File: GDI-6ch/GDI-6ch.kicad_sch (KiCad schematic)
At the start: 245 parts, among them J1 Conn_02x02_Odd_Even, J2 FTSH-107-01-F-DV-K, J3 TC2030, J4 Conn_01x06, J5 Conn_01x04, P1 368255-2, P10 Pad, P11 Pad, P18 Pad, P19 Pad, P2 Pad, P20 Pad, P25 Pad, P26 Pad, P27 Pad, P28 Pad, P29 Pad, P3 Pad, P30 Pad, P31 Pad, P32 Pad, P36 Pad, P4 Pad, P5 Pad, P6 Pad, P7 Pad, P8 Pad, P9 Pad, Q10 BUK9230-100B, Q11 BUK9230-100B, Q12 BUK9230-100B, Q13 AOD4185, Q14 VND14NV04TR-E, Q15 VND14NV04TR-E, Q2 BUK9230-100B, Q3 BUK9230-100B, Q4 BUK9230-100B, Q5 BUK9230-100B, Q6 BUK9230-100B, Q7 BUK9230-100B, Q8 BUK9230-100B, Q9 BUK9230-100B, U1 MC33816, U2 TJA1051T-3, U3 LM78M05_TO252, U4 74HC14, U5 XC6206P332MR, U6 MCP6004, U7 STM32F103C8Tx, Y2 1MHz

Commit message: Upd SCH
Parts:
- removed P11, P25, P26, P27, P28, P29, P30, P31, P6: Pad, hellen-one-common:PAD-TH, symbol hellen-one-common:Pad
- removed U1: MC33816, kicad6-libraries:LQFP-64-1EP_10x10mm_P0.5mm_EP5x5mm_ThermalVias, symbol chips:MC33816
- added C84, C85, C87, C88, C93, C94, C95, C96: 1000pF, Capacitor_SMD:C_0603_1608Metric, symbol Device:C
- added C86: 100n, hellen-one-common:C0603, symbol hellen-one-common:Cap
- added C89, C90, C91, C92: 4700p, hellen-one-common:C0603, symbol hellen-one-common:Cap
- added C97, C98: 0.33uF, Capacitor_SMD:C_0603_1608Metric, symbol Device:C
- added C99: 330p, hellen-one-common:C0603, symbol hellen-one-common:Cap
- added D17: SBR10200CTL, Package_TO_SOT_SMD:TO-252-2, symbol Device:D_Schottky_Dual_CommonCathode_AKA
- added D19, D22: STPS2H100UY, Diode_SMD:D_SMB, symbol Device:D_Schottky_Small
- added Q1, Q16, Q17, Q18: BUK9230-100B, Package_TO_SOT_SMD:TO-252-2, symbol Device:Q_NMOS_GDS
- added R37, R41, R84, R85, R86, R87: Jumper-Pad-Pad, hellen-one-common:PAD-0805-PAD, symbol hellen-one-common:Jumper-Pad-Pad
- added R88, R89: 1K, Resistor_SMD:R_0603_1608Metric, symbol Device:R
- added R90: 0.01, kicad6-libraries:Shunt_1206, symbol Device:R_Shunt
- added R91, R92, R93, R94: 10, Resistor_SMD:R_0603_1608Metric, symbol Device:R
- added R95, R96: DNP, hellen-one-common:PAD-0805-PAD, symbol hellen-one-common:Jumper-Pad-Pad
- added U1: 74HC14, Package_SO:TSSOP-14_4.4x5mm_P0.65mm, symbol 74xx:74HC14
- added U8: PT2000, kicad6-libraries:LQFP-80-1EP_12x12mm_P0.5mm, symbol chips:PT2000
- F1: LCSC C310989 -> C310992; MyComment 10A -> 20A
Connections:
- net +3V3: now also C86.2, R88.1, R89.1, U1.14 (VCC)
- net +5V: now also U8.22 (VCC5)
- net +BATT: now also Q1.2 (D), U8.47 (VBAT)
- net CLK: now also U8.80 (CLK)
- net CSB: now also U8.14 (CS)
- net DRVEN: now also U8.1 (DRVEN)
- net FLAG_0: now also U8.10 (FLAG0/EXTFW1)
- net GND: now also C84.1, C85.1, C86.1, C87.1, C88.1, C89.1, C90.1, C91.1, C92.1, D17.1 (A), R90.4, U1.11, U1.13, U1.5, U1.7 (GND), U1.9, U8.20 (DGND), U8.23 (AGND), U8.81 (PGND_(EXPOSED_PAD))
- net H1: now also U8.75 (S_HS2)
- net H3: now also U8.69 (S_HS4)
- net H5: now also C89.2, C90.2, C94.1, C98.2, D17.2 (K), Q16.3 (S), R85.2, R87.2, U8.63 (S_HS6); no longer C62.1, C64.2, C65.2, D15.1 (K), Q11.3 (S)
- net IN_PUMP1: now also C29.2, R27.2, RN2.4 (R4.1); no longer C18.2, R8.2, RN2.3 (R3.1)
- net IN_PUMP2: now also C18.2, R8.2, RN2.3 (R3.1); no longer C29.2, R27.2, RN2.4 (R4.1)
- net L1: now also U8.46 (D_LS1)
- net L2: now also U8.45 (D_LS2)
- net L3: now also U8.44 (D_LS3)
- net L4: now also U8.43 (D_LS4)
- net L5: now also C91.2, D19.2 (A), Q17.2 (D), R84.2, U8.42 (D_LS5); no longer C67.2, D16.2 (A), Q12.2 (D)
- net LS1: now also U7.45 (PB8); no longer U7.11 (PA1)
- net MISO: now also U8.16 (MISO)
- net MOSI: now also U8.15 (MOSI)
- net OA_1: now also U8.36 (OA_1)
- net OA_2: now also U8.37 (OA_2/FLAG_14)
- net RESETB: now also U8.2 (RESET)
- net SCLK: now also U8.17 (SCK)
- net START1: now also U8.3 (START1/FLAG_5)
- net START2: now also U8.4 (START2/FLAG_6)
- net START3: now also U8.5 (START3/FLAG_7)
- net START4: now also U8.6 (START4/FLAG_8)
- net START5: now also U8.7 (START5/FLAG_9)
- net START6: now also U8.8 (START6/FLAG_10)
- net VCCP: now also U8.48 (VCCP)
- net Vdrive: now also D19.1 (K), D22.1 (K), Q16.2 (D), U8.57 (VBOOST)
- net Vdrive_coil: now also U8.40 (D_LS7)
- net at C40.2, C56.1, D11.3 (A)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: now also U8.72 (S_HS3)
- net at C39.2, C52.1, D10.3 (A)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: now also U8.78 (S_HS1)
- net at C39.1: now also U8.76 (B_HS1)
- net FLAG_3: now reaches U7.38 (PA15)
- net FLAG_3: now also R96.2
- net at C51.2, D8.4, RN2.5 (R4.2): now also U1.3; no longer U4.13
- net at C10.2, R21.2: now also U8.27 (VSENSEP1)
- net at C10.1, R21.3: now also U8.26 (VSENSEN1)
- net at R81.1: now also U8.11 (FLAG1/EXTFW2)
- net at P1.45: now also R37.1
- net at P1.47: now also R41.1
- net at C13.1, R26.3: now also U8.30 (VSENSEN3)
- net at C13.2, R26.2: now also U8.31 (VSENSEP3)
- net at C59.2, R45.4: now also U8.18 (VCCIO)
- net at C24.1, R12.3: now also U8.32 (VSENSEN5)
- net at C24.2, R12.2: now also U8.33 (VSENSEP5)
- net OUT_INJ5_N: now reaches P1.117
- net OUT_INJ5_N: now also R86.1
- net OUT_INJ6_N: now reaches P1.115
- net OUT_INJ6_N: now also R84.1
- net OUT_INJ5_P: now reaches P1.116
- net OUT_INJ5_P: now also R85.1
- net OUT_INJ6_P: now reaches P1.120
- net OUT_INJ6_P: now also R87.1
- net IN_INJ5: now reaches RN2.1 (R1.1)
- net IN_INJ5: now also C84.2, R37.2, R88.2
- net IN_INJ6: now reaches RN2.2 (R2.1)
- net IN_INJ6: now also C85.2, R41.2, R89.2
- net at C37.2, D8.6, RN2.6 (R3.2): now also U1.1; no longer U4.11
- net at RN2.7 (R2.2): now also U4.13, C88.2
- net at RN2.8 (R1.2): now also U4.11, C87.2
- net at C32.2, C9.2: now also U8.21 (VCC2P5)
- net at R14.1: now also U8.55 (G_LS2)
- net at R11.1: now also U8.74 (G_HS2)
- net at R80.1: now also U8.79 (IRQ/FLAG_13)
- net at R10.1: now also U8.77 (G_HS1)
- net at C64.1: now also U8.58 (B_HS7)
- net at R82.1: now also U8.12 (FLAG2/EXTFW3)
- net at R83.1: now also U8.19 (DBG/FLAG_15)
- net at C11.1, R22.3: now also U8.28 (VSENSEN2)
- net at C11.2, R22.2: now also U8.29 (VSENSEP2)
- net at R24.2: now also U8.50 (G_LS7)
- net at R20.1: now also U8.49 (G_LS8)
- net at R18.1: now also U8.53 (G_LS4)
- net at R17.1: now also U8.54 (G_LS3)
- net at R13.1: now also U8.56 (G_LS1)
- net at R19.1: now also U8.59 (G_HS7)
- net at C42.1: now also U8.67 (B_HS4)
- net at R16.1: now also U8.68 (G_HS4)
- net at C40.1: now also U8.70 (B_HS3)
- net at R15.1: now also U8.71 (G_HS3)
- net at C41.1: now also U8.73 (B_HS2)
- net FLAG_4: now reaches U7.5 (PD0)
- net FLAG_4: now also R95.2
- new net: R91.1, U8.65 (G_HS5)
- new net: C93.2, Q1.1 (G), R91.2
- new net: C93.1, C97.2, D17.3 (A), Q1.3 (S), U8.66 (S_HS5)
- new net: R93.1, U8.52 (G_LS5)
- new net: C95.2, Q17.1 (G), R93.2
- new net: C96.2, Q18.1 (G), R94.2
- new net: C95.1, C96.1, Q17.3 (S), Q18.3 (S), R90.1
- new net: R95.1, U8.25 (VSENSEP4/FLAG_4)
- new net: R92.1, U8.62 (G_HS6)
- new net: C94.2, Q16.1 (G), R92.2
- new net: C98.1, U8.61 (B_HS6)
- new net: R94.1, U8.51 (G_LS6)
- new net: C97.1, U8.64 (B_HS5)
- new net: C99.1, R90.3, U8.34 (VSENSEN6)
- new net: C99.2, R90.2, U8.35 (VSENSEP6)
- new net: R96.1, U8.13 (FLAG3/EXTFW4)
- new net H7: C62.1, C64.2, C65.2, D15.1 (K), Q11.3 (S), U8.60 (S_HS7)
- new net L6: C92.2, D22.2 (A), Q18.2 (D), R86.2, U8.41 (D_LS6)
- new net L7: C67.2, D16.2 (A), Q12.2 (D), U8.39 (D_LS8)
- new net OA_3: U7.11 (PA1), U8.38 (OA_3/D_HS1_7)
- new net START7: U1.2, U8.9 (START7/FLAG_11)
- new net START8: U1.4, U8.24 (VSENSEN4/START8/FLAG_12)
- no-connect marks 93 -> 92
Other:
- note added: "INJECTOR BANK 3"
- note removed: "rev. a: STTH802G-TR"
- moved on the sheet: C10, C11, C12, C13, C14, C15, C16, C17, C21, C22, C23, C24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

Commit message: Fixed #101
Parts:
- added J10: Conn_01x01, MountingHole:MountingHole_4.5mm, symbol Connector_Generic:Conn_01x01
- added J6, J7: Conn_01x01, MountingHole:MountingHole_3.5mm, symbol Connector_Generic:Conn_01x01
- added J8, J9: Conn_01x01, MountingHole:MountingHole_5.5mm, symbol Connector_Generic:Conn_01x01
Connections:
- net H5: no longer R75.2
- net H7: now also R74.2
- net L5: no longer R74.2
- net L7: now also R75.2
- no-connect marks 92 -> 97
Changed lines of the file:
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@@
   (junction (at 240.03 337.82) (diameter 0) (color 0 0 0 0)
   )
+  (no_connect (at 26.67 374.65))
   (no_connect (at 44.45 177.8))
   (no_connect (at 543.56 85.09))
@@
   (no_connect (at 151.13 284.48))
   (no_connect (at 151.13 279.4))
+  (no_connect (at 26.67 377.19))
+  (no_connect (at 26.67 384.81))
+  (no_connect (at 26.67 379.73))
   (no_connect (at 556.26 85.09))
   (no_connect (at 44.45 190.5))
@@
   (no_connect (at 546.1 129.54))
   (no_connect (at 556.26 106.68))
+  (no_connect (at 26.67 382.27))
   (no_connect (at 44.45 314.96))
   (no_connect (at 44.45 317.5))
@@
     (effects (font (size 1.524 1.524)) (justify left bottom))
   )
-  (label "L5" (at 69.85 269.24 0)
+  (label "H7" (at 69.85 269.24 0)
     (effects (font (size 1.524 1.524)) (justify left bottom))
   )
@@
     (effects (font (size 1.524 1.524)) (justify left bottom))
   )
-  (label "H5" (at 69.85 274.32 0)
+  (label "L7" (at 69.85 274.32 0)
     (effects (font (size 1.524 1.524)) (justify left bottom))
   )
@@
     (pin "1")
   )
+  (symbol (lib_id "Connector_Generic:Conn_01x01") (at 21.59 379.73 0) (mirror y) (unit 1)
+    (in_bom yes) (on_board yes)
+    (property "Reference" "J8" (id 0) (at 19.558 379.8316 0)
+      (effects (font (size 1.27 1.27)) (justify left))
+    )
+    (property "Value" "Conn_01x01" (id 1) (at 19.558 380.9746 0)
+      (effects (font (size 1.27 1.27)) (justify left) hide)
+    )
+    (property "Footprint" "MountingHole:MountingHole_5.5mm" (id 2) (at 21.59 379.73 0)
+      (effects (font (size 1.27 1.27)) hide)
+    )
+    (property "Datasheet" "~" (id 3) (at 21.59 379.73 0)
+      (effects (font (size 1.27 1.27)) hide)
+    )
+    (pin "1")
+  )
   (symbol (lib_id "semiconductors:VND14NV04TR-E") (at 132.08 120.65 0) (mirror y) (unit 1)
     (in_bom yes) (on_board yes) (fields_autoplaced)
@@
     (pin "1")
   )
+  (symbol (lib_id "Connector_Generic:Conn_01x01") (at 21.59 377.19 0) (mirror y) (unit 1)
+    (in_bom yes) (on_board yes)
+    (property "Reference" "J7" (id 0) (at 19.558 377.2916 0)
+      (effects (font (size 1.27 1.27)) (justify left))
+    )
+    (property "Value" "Conn_01x01" (id 1) (at 19.558 378.4346 0)
+      (effects (font (size 1.27 1.27)) (justify left) hide)
+    )
+    (property "Footprint" "MountingHole:MountingHole_3.5mm" (id 2) (at 21.59 377.19 0)
+      (effects (font (size 1.27 1.27)) hide)
+    )
+    (property "Datasheet" "~" (id 3) (at 21.59 377.19 0)
+      (effects (font (size 1.27 1.27)) hide)
+    )
+    (pin "1")
+  )
   (symbol (lib_id "hellen-one-common:Cap") (at 492.76 241.3 90) (unit 1)
     (in_bom yes) (on_board yes)
@@
     (pin "2")
   )
+  (symbol (lib_id "Connector_Generic:Conn_01x01") (at 21.59 374.65 0) (mirror y) (unit 1)
+    (in_bom yes) (on_board yes)
+    (property "Reference" "J6" (id 0) (at 19.558 374.7516 0)
+      (effects (font (size 1.27 1.27)) (justify left))
+    )
+    (property "Value" "Conn_01x01" (id 1) (at 19.558 375.8946 0)
+      (effects (font (size 1.27 1.27)) (justify left) hide)
+    )
+    (property "Footprint" "MountingHole:MountingHole_3.5mm" (id 2) (at 21.59 374.65 0)
+      (effects (font (size 1.27 1.27)) hide)
+    )
+    (property "Datasheet" "~" (id 3) (at 21.59 374.65 0)
+      (effects (font (size 1.27 1.27)) hide)
+    )
+    (pin "1")
+  )
   (symbol (lib_id "power:Vdrive") (at 516.89 229.87 0) (unit 1)
     (in_bom yes) (on_board yes)
@@
     (pin "1")
   )
+  (symbol (lib_id "Connector_Generic:Conn_01x01") (at 21.59 382.27 0) (mirror y) (unit 1)
+    (in_bom yes) (on_board yes)
+    (property "Reference" "J9" (id 0) (at 19.558 382.3716 0)
+      (effects (font (size 1.27 1.27)) (justify left))
+    )
+    (property "Value" "Conn_01x01" (id 1) (at 19.558 383.5146 0)
+      (effects (font (size 1.27 1.27)) (justify left) hide)
+    )
+    (property "Footprint" "MountingHole:MountingHole_5.5mm" (id 2) (at 21.59 382.27 0)
+      (effects (font (size 1.27 1.27)) hide)
+    )
+    (property "Datasheet" "~" (id 3) (at 21.59 382.27 0)
+      (effects (font (size 1.27 1.27)) hide)
+    )
+    (pin "1")
+  )
   (symbol (lib_id "hellen-one-common:Cap") (at 175.26 350.52 270) (mirror x) (unit 1)
     (in_bom yes) (on_board yes)
@@
     (pin "1")
   )
+  (symbol (lib_id "Connector_Generic:Conn_01x01") (at 21.59 384.81 0) (mirror y) (unit 1)
+    (in_bom yes) (on_board yes)
+    (property "Reference" "J10" (id 0) (at 19.558 384.9116 0)
+      (effects (font (size 1.27 1.27)) (justify left))
+    )
+    (property "Value" "Conn_01x01" (id 1) (at 19.558 386.0546 0)
+      (effects (font (size 1.27 1.27)) (justify left) hide)
+    )
+    (property "Footprint" "MountingHole:MountingHole_4.5mm" (id 2) (at 21.59 384.81 0)
+      (effects (font (size 1.27 1.27)) hide)
+    )
+    (property "Datasheet" "~" (id 3) (at 21.59 384.81 0)
+      (effects (font (size 1.27 1.27)) hide)
+    )
+    (pin "1")
+  )
   (symbol (lib_id "hellen-one-common:Jumper-Pad-Pad") (at 64.77 302.26 0) (unit 1)
     (in_bom yes) (on_board yes)
@@
       (reference "J5") (unit 1) (value "Conn_01x04") (footprint "Connector_PinHeader_2.54mm:PinHeader_1x04_P2.54mm_Vertical")
     )
+    (path "/3d0bfdb4-f915-4e5b-8546-3740a7f922a9"
+      (reference "J6") (unit 1) (value "Conn_01x01") (footprint "MountingHole:MountingHole_3.5mm")
+    )
+    (path "/26c9a61b-49de-43ad-b3c9-7b4385b6b4c9"
+      (reference "J7") (unit 1) (value "Conn_01x01") (footprint "MountingHole:MountingHole_3.5mm")
+    )
+    (path "/222d138c-e7d2-44f4-9190-3b43b3d80d22"
+      (reference "J8") (unit 1) (value "Conn_01x01") (footprint "MountingHole:MountingHole_5.5mm")
+    )
+    (path "/a95c9cf3-e7f6-4e55-af82-e835c376a250"
+      (reference "J9") (unit 1) (value "Conn_01x01") (footprint "MountingHole:MountingHole_5.5mm")
+    )
+    (path "/b62e8ad9-bb27-42dc-95bd-43b459f6fa8f"
+      (reference "J10") (unit 1) (value "Conn_01x01") (footprint "MountingHole:MountingHole_4.5mm")
+    )
     (path "/00000000-0000-0000-0000-00005a78864f"

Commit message: GDI-6ch upd pcb
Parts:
- F1: LCSC C310992 -> C310989; MyComment 20A -> 10A
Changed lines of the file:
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@@
     (pin "2")
   )
-  (symbol (lib_id "hellen-one-common:Fuse-Pad-Pad") (at 57.15 24.13 0) (unit 1)
-    (in_bom yes) (on_board yes)
-    (property "Reference" "F1" (id 0) (at 57.15 21.59 0)
-      (effects (font (size 1.016 1.016)))
-    )
-    (property "Value" "Fuse-Pad-Pad" (id 1) (at 57.15 25.908 0)
-      (effects (font (size 1.016 1.016)) hide)
-    )
-    (property "Footprint" "hellen-one-common:PAD-1206-PAD" (id 2) (at 57.15 27.94 0)
-      (effects (font (size 1.524 1.524)) hide)
-    )
-    (property "Datasheet" "" (id 3) (at 57.15 24.13 0)
-      (effects (font (size 1.524 1.524)) hide)
-    )
-    (property "LCSC" "C310992" (id 4) (at 57.15 27.94 0)
-      (effects (font (size 1.27 1.27)) hide)
-    )
-    (property "MyComment" "20A" (id 5) (at 57.15 26.67 0)
-      (effects (font (size 1.524 1.524)))
-    )
-    (pin "1")
-    (pin "2")
-  )
   (symbol (lib_id "Device:C") (at 341.63 280.67 270) (mirror x) (unit 1)
     (in_bom yes) (on_board yes)
@@
     (pin "1")
   )
+  (symbol (lib_id "hellen-one-common:Fuse-Pad-Pad") (at 57.15 24.13 0) (unit 1)
+    (in_bom yes) (on_board yes)
+    (property "Reference" "F1" (id 0) (at 57.15 21.59 0)
+      (effects (font (size 1.016 1.016)))
+    )
+    (property "Value" "Fuse-Pad-Pad" (id 1) (at 57.15 25.908 0)
+      (effects (font (size 1.016 1.016)) hide)
+    )
+    (property "Footprint" "hellen-one-common:PAD-1206-PAD" (id 2) (at 57.15 27.94 0)
+      (effects (font (size 1.524 1.524)) hide)
+    )
+    (property "Datasheet" "" (id 3) (at 57.15 24.13 0)
+      (effects (font (size 1.524 1.524)) hide)
+    )
+    (property "LCSC" "C310989" (id 4) (at 57.15 27.94 0)
+      (effects (font (size 1.27 1.27)) hide)
+    )
+    (property "MyComment" "10A" (id 5) (at 57.15 26.67 0)
+      (effects (font (size 1.524 1.524)))
+    )
+    (pin "1")
+    (pin "2")
+  )
   (symbol (lib_id "Device:R") (at 116.84 351.79 0) (unit 1)
     (in_bom yes) (on_board yes)
@@
       (reference "D34") (unit 1) (value "SDURB1020CT") (footprint "Package_TO_SOT_SMD:TO-263-2")
     )
-    (path "/48fdf64d-2991-45af-8fbb-4a90125d1485"
+    (path "/686018fd-d436-4cab-b284-2f8048ed362a"
       (reference "F1") (unit 1) (value "Fuse-Pad-Pad") (footprint "hellen-one-common:PAD-1206-PAD")
     )

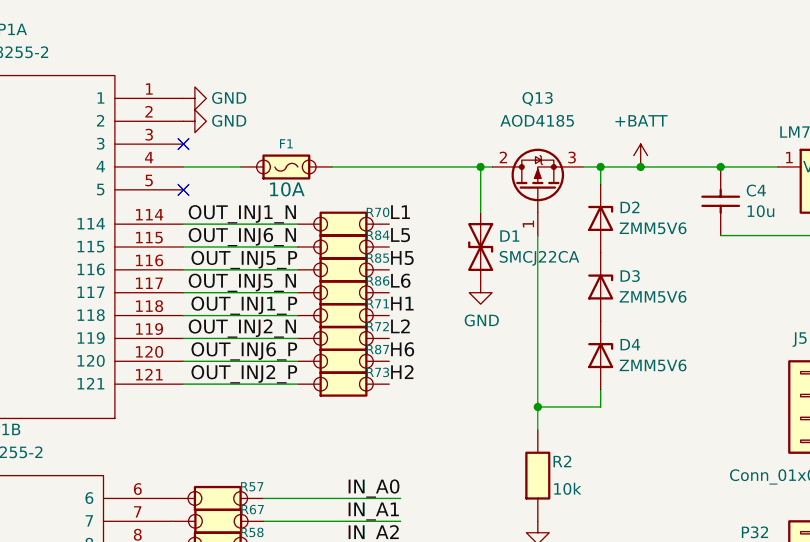
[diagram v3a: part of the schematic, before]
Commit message: Upd sch & pcb GDI4 -> 6
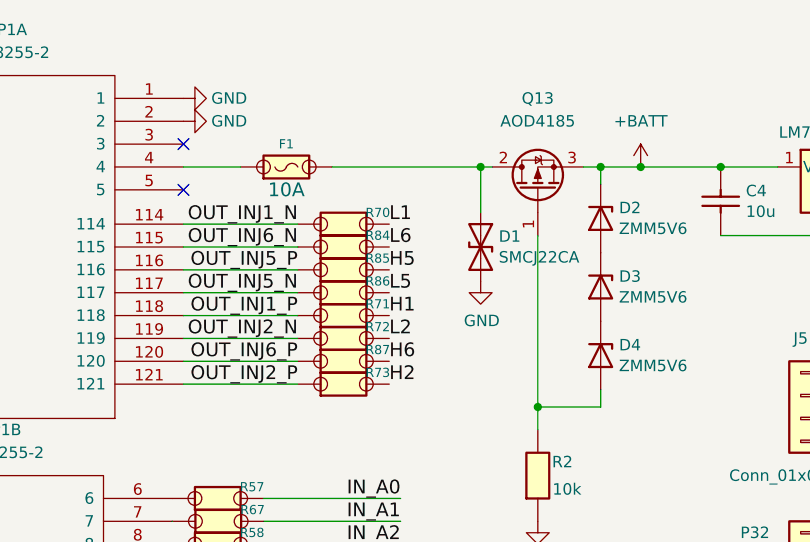
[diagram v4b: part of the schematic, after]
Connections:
- net L5: now also R86.2; no longer R84.2
- net L6: now also R84.2; no longer R86.2
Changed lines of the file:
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@@
     (effects (font (size 1.524 1.524)) (justify right bottom))
   )
-  (label "L6" (at 68.58 38.1 0)
+  (label "L6" (at 68.58 33.02 0)
     (effects (font (size 1.524 1.524)) (justify left bottom))
   )
@@
     (effects (font (size 1.524 1.524)) (justify left bottom))
   )
-  (label "L5" (at 68.58 33.02 0)
+  (label "L5" (at 68.58 38.1 0)
     (effects (font (size 1.524 1.524)) (justify left bottom))
   )

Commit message: Upd GDI6
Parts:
- removed R45: 0.01, kicad6-libraries:Shunt_1206, symbol Device:R_Shunt
- added R100, R101, R102, R103, R104, R105, R106, R97, R99: 56k, Resistor_SMD:R_0805_2012Metric, symbol Device:R
- added R45, R98: 2K, Resistor_SMD:R_1206_3216Metric, symbol Device:R
- J10, J6, J7, J8, J9: symbol Connector_Generic:Conn_01x01 -> Mechanical:MountingHole; now left out of the parts list
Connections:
- net +3V3: now also C59.2, U8.18 (VCCIO)
- net +Batt_filtered: now also R45.1, R98.1
- net GND: now also R45.2, R98.2
- net Vdrive: now also R100.1, R101.1, R102.1, R103.1, R104.1, R105.1, R106.1, R97.1, R99.1
- net Vdrive_shunt: now also R100.2, R101.2, R102.2, R103.2, R104.2, R105.2, R106.2, R97.2, R99.2
- net at C88.2, RN2.7 (R2.2), U4.13: now also D8.1
- net at C87.2, RN2.8 (R1.2), U4.11: now also D8.3
- no-connect marks 97 -> 88
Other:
- note added: "Discharge circuit"
- title: GDI 4ch -> GDI 6ch

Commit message: GDI6 export
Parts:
- removed J10: Conn_01x01, MountingHole:MountingHole_4.5mm, symbol Mechanical:MountingHole
- removed P10, P18, P19, P2, P20, P3, P32, P36, P4, P5, P7, P8, P9: Pad, hellen-one-common:PAD-TH, symbol hellen-one-common:Pad
- added J11: Conn_01x08, Connector_PinHeader_2.54mm:PinHeader_1x08_P2.54mm_Vertical, symbol Connector_Generic:Conn_01x08
- added J12: Conn_01x04, Connector_PinHeader_2.54mm:PinHeader_1x04_P2.54mm_Vertical, symbol Connector_Generic:Conn_01x04
- C14, C15, C16, C21, C22, C25, C27, C83: value 390uF -> 470uF; footprint Capacitor_SMD:CP_Elec_16x17.5 -> Capacitor_THT:CP_Radial_D16.0mm_P7.50mm; LCSC C487421 -> C443092
- C17, C80, C81, C82: LCSC C342873 -> C513710
- C43, C44, C45, C46, C47, C48, C49, C50, C65, C67, C89, C90, C91, C92: LCSC C342899 -> C327158
- D1: LCSC C310038 -> C151904
- D2, D3, D4: LCSC C8062 -> C7497481
- D20: LCSC C72041 -> C497940
- D21: LCSC C72043 -> C965804
- D34: value SDURB1020CT -> STTH802G-TR; LCSC C260365 -> C181034
- F1: LCSC C310989 -> C136354
- J1, J2, J3, J4: now not fitted
- J5: value Conn_01x04 -> Conn_01x05; footprint Connector_PinHeader_2.54mm:PinHeader_1x04_P2.54mm_Vertical -> Connector_PinHeader_2.54mm:PinHeader_1x05_P2.54mm_Vertical; symbol Connector_Generic:Conn_01x04 -> Connector_Generic:Conn_01x05
- L1: LCSC C380073 -> C149517
- Y2: LCSC C70608 -> C2901463
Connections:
- net +3V3: now also J5.4 (Pin_4); no longer J5.3 (Pin_3)
- net +5V: now also J5.3 (Pin_3); no longer J5.2 (Pin_2)
- net +BATT: now also J5.2 (Pin_2); no longer J5.1 (Pin_1)
- net Boot0: now also J11.5 (Pin_5)
- net CSB: now also J12.4 (Pin_4)
- net DRVEN: now also J11.8 (Pin_8)
- net FLAG_0: now also J11.6 (Pin_6)
- net GND: now also J5.5 (Pin_5); no longer J5.4 (Pin_4)
- net MISO: now also J12.2 (Pin_2)
- net MOSI: now also J12.3 (Pin_3)
- net RESETB: now also J11.7 (Pin_7)
- net SCLK: now also J12.1 (Pin_1)
- net Vdrive: now also J5.1 (Pin_1)
- net C13: now reaches U7.2 (PC13)
- net C13: now also J11.4 (Pin_4)
- net C14: now reaches U7.3 (PC14)
- net C14: now also J11.3 (Pin_3)
- net D1: now reaches U7.6 (PD1)
- net D1: now also J11.1 (Pin_1)
- net C15: now reaches U7.4 (PC15)
- net C15: now also J11.2 (Pin_2)

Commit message: GDI 6 rev b
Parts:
- removed F1: Fuse-Pad-Pad, hellen-one-common:PAD-1206-PAD, symbol hellen-one-common:Fuse-Pad-Pad
- removed R37, R41, R56, R57, R58, R59, R61, R62, R63, R64, R65, R66, R67, R68, R69, R70, R71, R72, R73, R74, R75, R76, R77, R78, R79, R84, R85, R86, R87: Jumper-Pad-Pad, hellen-one-common:PAD-0805-PAD, symbol hellen-one-common:Jumper-Pad-Pad
- added F1: 10A, Fuse:Fuse_1206_3216Metric, symbol Device:Fuse
- added J10: Conn_01x08, Connector_PinHeader_2.54mm:PinHeader_1x08_P2.54mm_Vertical, symbol Connector_Generic:Conn_01x08
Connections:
- net OUT_INJ1_N is gone; now on net L1: P1.114
- net OUT_INJ1_P is gone; now on net H1: P1.118
- net OUT_INJ2_N is gone; now on net L2: P1.119
- net OUT_INJ2_P is gone; now on net H1: P1.121
- net OUT_INJ3_N is gone; now on net L3: P1.90, P1.91
- net OUT_INJ3_P is gone; now on net H3: P1.94, P1.95
- net OUT_INJ4_N is gone; now on net L4: P1.92, P1.93
- net OUT_INJ4_P is gone; now on net H3: P1.96, P1.97
- net OUT_INJ5_N is gone; now on net L5: P1.117
- net OUT_INJ5_P is gone; now on net H5: P1.116
- net OUT_INJ6_N is gone; now on net L6: P1.115
- net OUT_INJ6_P is gone; now on net H5: P1.120
- net OUT_PUMP_N is gone; now on net H7: P1.82, P1.83
- net OUT_PUMP_P is gone; now on net L7: P1.84, P1.85
- net CAN_H: now also P1.52
- net CAN_L: now also P1.53
- net IN_A0: now also P1.6
- net IN_A1: now also P1.7
- net IN_A2: now also P1.8
- net IN_A3: now also P1.9
- net IN_INJ1: now also P1.44
- net IN_INJ2: now also P1.48
- net IN_INJ3: now also P1.46
- net IN_INJ4: now also P1.49
- net IN_INJ5: now also P1.45
- net IN_INJ6: now also P1.47
- net IN_PUMP1: now also P1.41
- net OUT_LS1: now also P1.21, P1.22
- net OUT_LS2: now also P1.23, P1.24
- net START1: now also J10.1 (Pin_1)
- net START2: now also J10.2 (Pin_2)
- net START3: now also J10.3 (Pin_3)
- net START4: now also J10.4 (Pin_4)
- net START5: now also J10.5 (Pin_5)
- net START6: now also J10.6 (Pin_6)
- net START7: now also J10.7 (Pin_7)
- net START8: now also J10.8 (Pin_8)
- net at P1.4: now also F1.1
- net at D1.1 (A1), Q13.2 (D): now also F1.2
